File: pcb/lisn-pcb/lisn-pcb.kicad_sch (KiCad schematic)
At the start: 28 parts, among them J1 Conn_Coaxial, J2 Conn_Coaxial, J3 62409-1, J4 62409-1, J5 62409-1, J6 62409-1, J7 62409-1, J8 62409-1, J9 62409-1

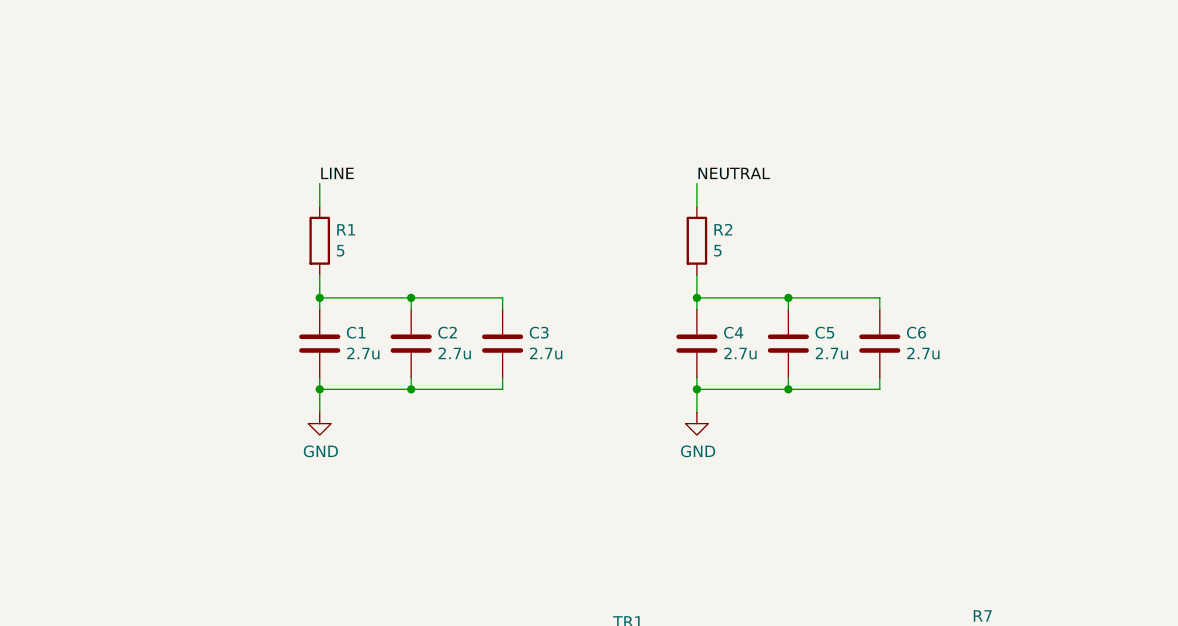
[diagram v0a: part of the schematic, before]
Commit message: Add bleed resistors
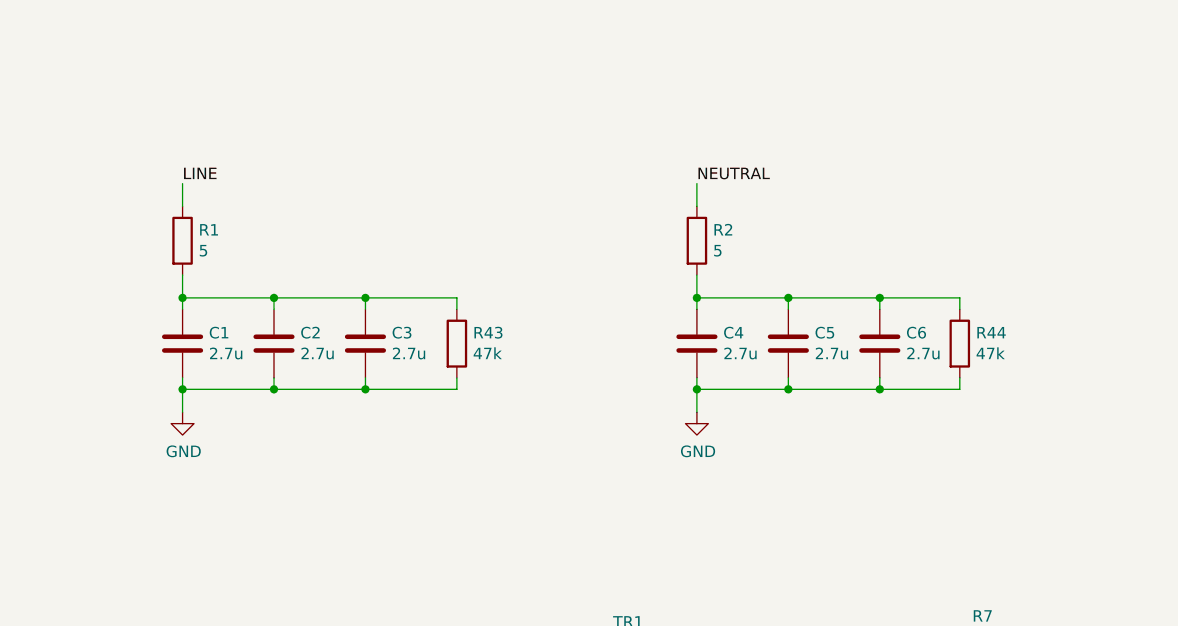
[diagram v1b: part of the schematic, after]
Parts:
- added R43, R44: 47k, Resistor_THT:R_Axial_DIN0414_L11.9mm_D4.5mm_P15.24mm_Horizontal, symbol Device:R
- R3: Manufacturer Part Number 1 RNCP0805FTD49R9 -> RNCP0805FTD49R9
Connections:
- net GND: now also R43.2, R44.2
- net at C1.1, C2.1, C3.1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: now also R43.1
- net at C4.1, C5.1, C6.1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: now also R44.1
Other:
- moved on the sheet: C1, C2, C3, R1

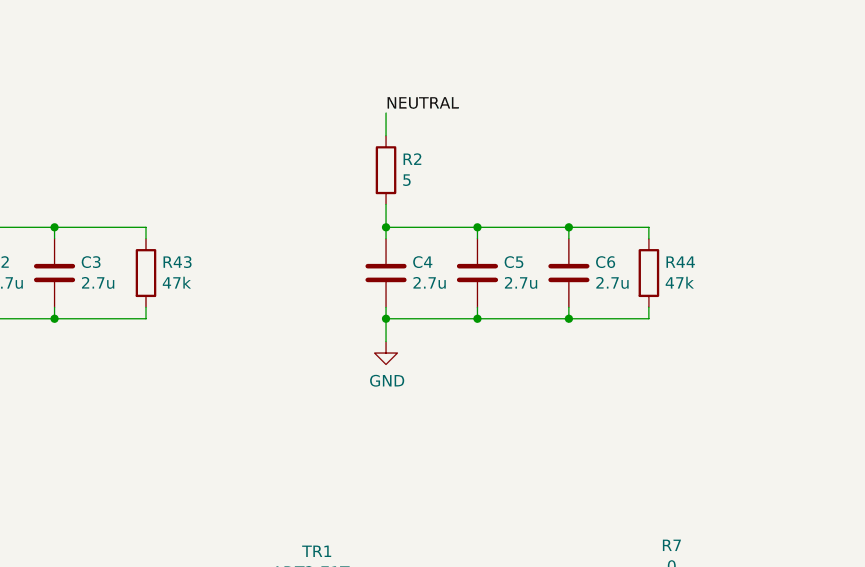
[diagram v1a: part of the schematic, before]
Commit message: Use a larger value for the bleed resistors
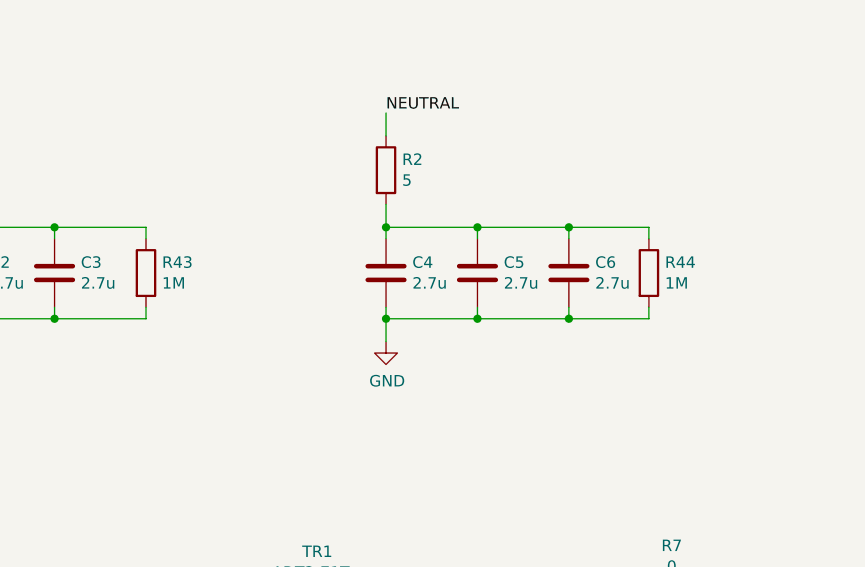
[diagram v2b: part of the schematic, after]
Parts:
- R43, R44: value 47k -> 1M; MPN ROX1SJ47K -> ROX1SJ1M0; Manufacturer Part Number 1 ROX1SJ47K -> ROX1SJ1M0; Price 1.66 -> .2; Supplier Part Number 1 279-ROX1SJ47K -> 279-ROX1SJ1M0
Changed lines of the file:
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@@
 			)
 		)
-		(property "Value" "47k"
+		(property "Value" "1M"
 			(at 144.018 59.563 0)
 			(effects
@@
 			)
 		)
-		(property "MPN" "ROX1SJ47K"
+		(property "MPN" " ROX1SJ1M0"
 			(at 142.24 58.42 0)
 			(effects
@@
 			)
 		)
-		(property "Manufacturer Part Number 1" "ROX1SJ47K"
-			(at 142.24 58.42 0)
-			(effects
-				(font
-					(size 1.27 1.27)
-				)
-				(hide yes)
-			)
-		)
-		(property "Price" "1.66"
+		(property "Manufacturer Part Number 1" " ROX1SJ1M0"
+			(at 142.24 58.42 0)
+			(effects
+				(font
+					(size 1.27 1.27)
+				)
+				(hide yes)
+			)
+		)
+		(property "Price" ".2"
 			(at 142.24 58.42 0)
 			(effects
@@
 			)
 		)
-		(property "Supplier Part Number 1" " 279-ROX1SJ47K"
+		(property "Supplier Part Number 1" " 279-ROX1SJ1M0"
 			(at 142.24 58.42 0)
 			(effects
@@
 			)
 		)
-		(property "Value" "47k"
+		(property "Value" "1M"
 			(at 199.898 59.563 0)
 			(effects
@@
 			)
 		)
-		(property "MPN" "ROX1SJ47K"
+		(property "MPN" "ROX1SJ1M0"
 			(at 198.12 58.42 0)
 			(effects
@@
 			)
 		)
-		(property "Manufacturer Part Number 1" "ROX1SJ47K"
-			(at 198.12 58.42 0)
-			(effects
-				(font
-					(size 1.27 1.27)
-				)
-				(hide yes)
-			)
-		)
-		(property "Price" "1.66"
+		(property "Manufacturer Part Number 1" "ROX1SJ1M0"
+			(at 198.12 58.42 0)
+			(effects
+				(font
+					(size 1.27 1.27)
+				)
+				(hide yes)
+			)
+		)
+		(property "Price" ".2"
 			(at 198.12 58.42 0)
 			(effects
@@
 			)
 		)
-		(property "Supplier Part Number 1" " 279-ROX1SJ47K"
-			(at 198.12 58.42 0)
-			(effects
+		(property "Supplier Part Number 1" "279-ROX1SJ1M0"
+			(at 198.12 58.42 0)
+			(effects
